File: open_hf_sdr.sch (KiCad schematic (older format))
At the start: 0 parts

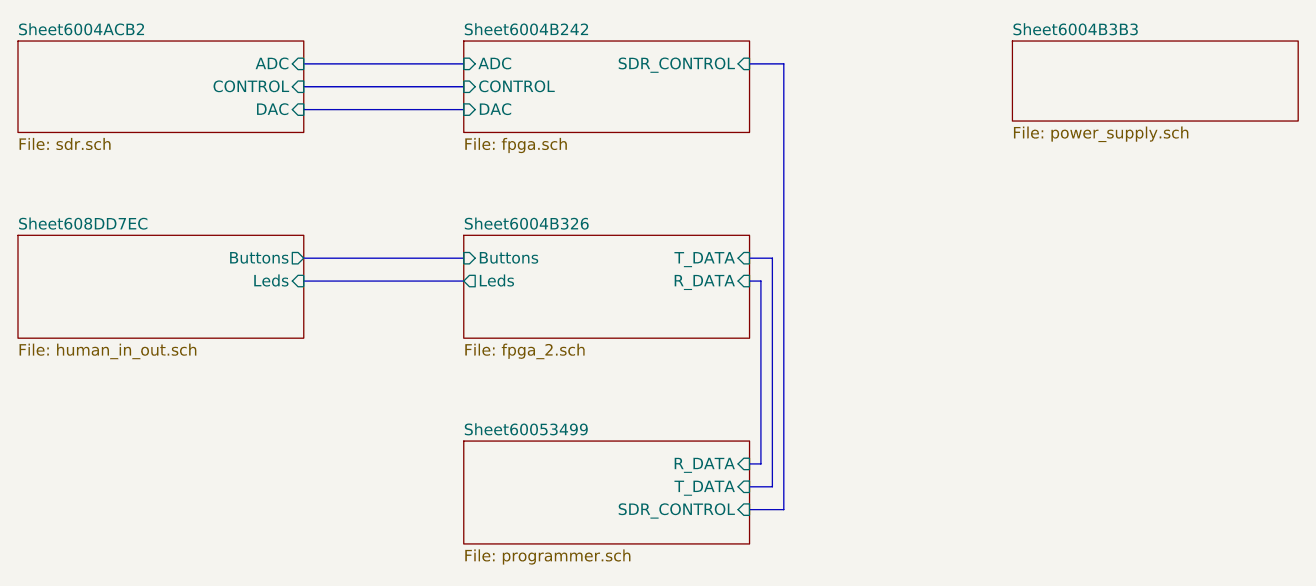
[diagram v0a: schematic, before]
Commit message: Add battery monitoring, and reverse polarity check
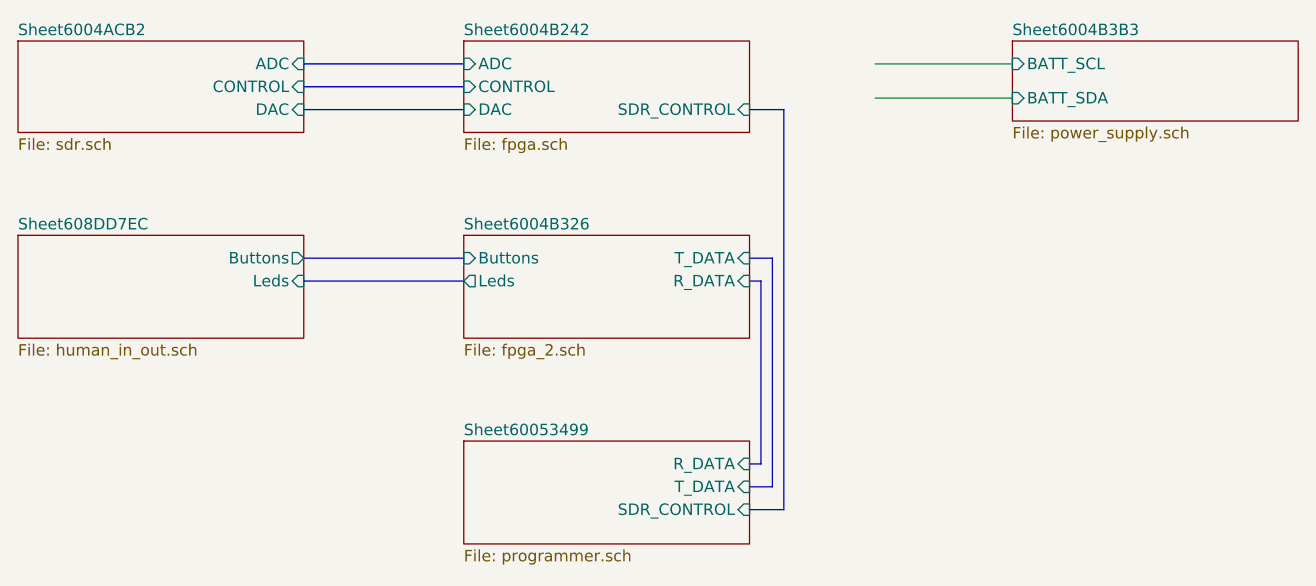
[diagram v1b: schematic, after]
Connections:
- wire segments 0 -> 2
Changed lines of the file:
@@
 F3 "DAC" I L 4450 2850 50
 F4 "CONTROL" I L 4450 2750 50
-F5 "SDR_CONTROL" I R 5700 2650 50
+F5 "SDR_CONTROL" I R 5700 2850 50
 $EndSheet
 $Sheet
@@
 F0 "Sheet6004B3B3" 50
 F1 "power_supply.sch" 50
+F2 "BATT_SCL" I L 6850 2650 50
+F3 "BATT_SDA" I L 6850 2800 50
 $EndSheet
 $Sheet
@@
 	5700 4600 5850 4600
 Wire Bus Line
-	5850 4600 5850 2650
+	5850 4600 5850 2850
 Wire Bus Line
-	5850 2650 5700 2650
+	5850 2850 5700 2850
+Wire Wire Line
+	6850 2650 6250 2650
+Wire Wire Line
+	6850 2800 6250 2800
 $EndSCHEMATC
